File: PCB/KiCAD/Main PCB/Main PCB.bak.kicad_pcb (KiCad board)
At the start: 2 copper layers, 120 x 120 mm, 144 parts, among them IC1 ADG608BRZ, IC2 ADG608BRZ, IC3 XB3-24Z8CM, J1 Conn_01x02, J2 Conn_01x02, J3 Conn_01x02, J4 Conn_Coaxial_Small, J5 Conn_01x02, J6 Conn_01x04, J7 Conn_01x04, M1 Conn_01x02_Pin, M2 Conn_01x02_Pin, M3 Conn_01x02_Pin, M4 Conn_01x02_Pin, Q1 BSS138, Q2 BSS138, U2 Teensy4.1, U3 Teensy4.0, U4 LMD18200, U5 LMD18200, U6 LMD18200, U7 LMD18200, U8 MIC5219-3.3YM5

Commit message: Changes to the main PCB
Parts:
- moved J6 4.50 mm to (-29.5, 31.0)
- moved J7 4.50 mm to (23.5, 31.0)
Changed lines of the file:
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@@
 	(footprint "Connector_JST:JST_PH_B4B-PH-K_1x04_P2.00mm_Vertical"
 		(layer "B.Cu")
-		(at -29.5 26.5)
+		(at -29.5 31)
 		(descr "JST PH series connector, B4B-PH-K (http://www.jst-mfg.com/product/pdf/eng/ePH.pdf), generated with kicad-footprint-generator")
 		(tags "connector JST PH side entry")
@@
 	(footprint "Connector_JST:JST_PH_B4B-PH-K_1x04_P2.00mm_Vertical"
 		(layer "B.Cu")
-		(at 23.5 26.5)
+		(at 23.5 31)
 		(descr "JST PH series connector, B4B-PH-K (http://www.jst-mfg.com/product/pdf/eng/ePH.pdf), generated with kicad-footprint-generator")
 		(tags "connector JST PH side entry")

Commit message: Updated to main PCB
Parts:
- added J8: Conn_01x04, Connector_JST:JST_PH_B4B-PH-K_1x04_P2.00mm_Vertical, F.Cu at (29.0, 14.5)
- moved J6 4.50 mm to (-29.5, 26.5)
- moved J7 4.50 mm to (23.5, 26.5)
- turned D10 to 158 degrees
- turned D12 to 113 degrees
- turned D14 to 68 degrees
- turned D16 to 23 degrees
- turned D18 to -22 degrees
- turned D20 to -67 degrees
- turned D22 to -112 degrees
- turned D24 to -157 degrees
- turned IR10 to -22 degrees
- turned IR12 to -67 degrees
- turned IR14 to -112 degrees
- turned IR16 to -157 degrees
- turned IR2 to 158 degrees
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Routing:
- net GND: track 77.1 -> 964.7 mm, vias 0 -> 1
- net TSSP_PWR: track 0.00 -> 410.8 mm, vias 0 -> 4
- net +3V3: track 0.00 -> 215.3 mm, vias 0 -> 6
- net +5V: track 0.00 -> 163.3 mm, vias 0 -> 3
- net IR_DIR_157.5: track 0.00 -> 158.9 mm, vias 0 -> 3
- net LG_RECEIVE: track 0.00 -> 154.4 mm, vias 0 -> 6
- net +3V3_4_0: track 0.00 -> 147.5 mm, vias 0 -> 8
- net START_BUTTON: track 0.00 -> 137.2 mm, vias 0 -> 2
- net LED_2_A2: track 0.00 -> 134.7 mm, vias 0 -> 2
- net +3V3_4_1: track 0.00 -> 132.3 mm, vias 0 -> 5
- net 3V3_SDA: track 0.00 -> 125.4 mm, vias 0 -> 3
- net IR_DIR_112.5: track 0.00 -> 119.7 mm, vias 0 -> 1
- net IR_DIR_180: track 0.00 -> 119.6 mm, vias 0 -> 4
- net 3V3_SCL: track 0.00 -> 114.3 mm, vias 0 -> 4
- net CAMERA_TX: track 0.00 -> 109.3 mm, vias 0 -> 3
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- removed copper zone on B.Cu, net GND
- removed copper zone on F.Cu, net GND

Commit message: More PCB updates
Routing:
- net Net-(IC2-S3): track 64.7 -> 65.7 mm
- net START_BUTTON: track 137.2 -> 136.2 mm
- net MOTOR_4_SPEED: track 60.3 -> 61.3 mm
- net MOTOR_3_SPEED: track 65.4 -> 64.6 mm
- net LED_1_A0: track 86.2 -> 86.9 mm
- net Net-(IC1-S4): track 59.3 -> 59.9 mm
- net Net-(IC1-S1): track 55.2 -> 55.9 mm
- net LED_2_A1: track 104.7 -> 104.1 mm

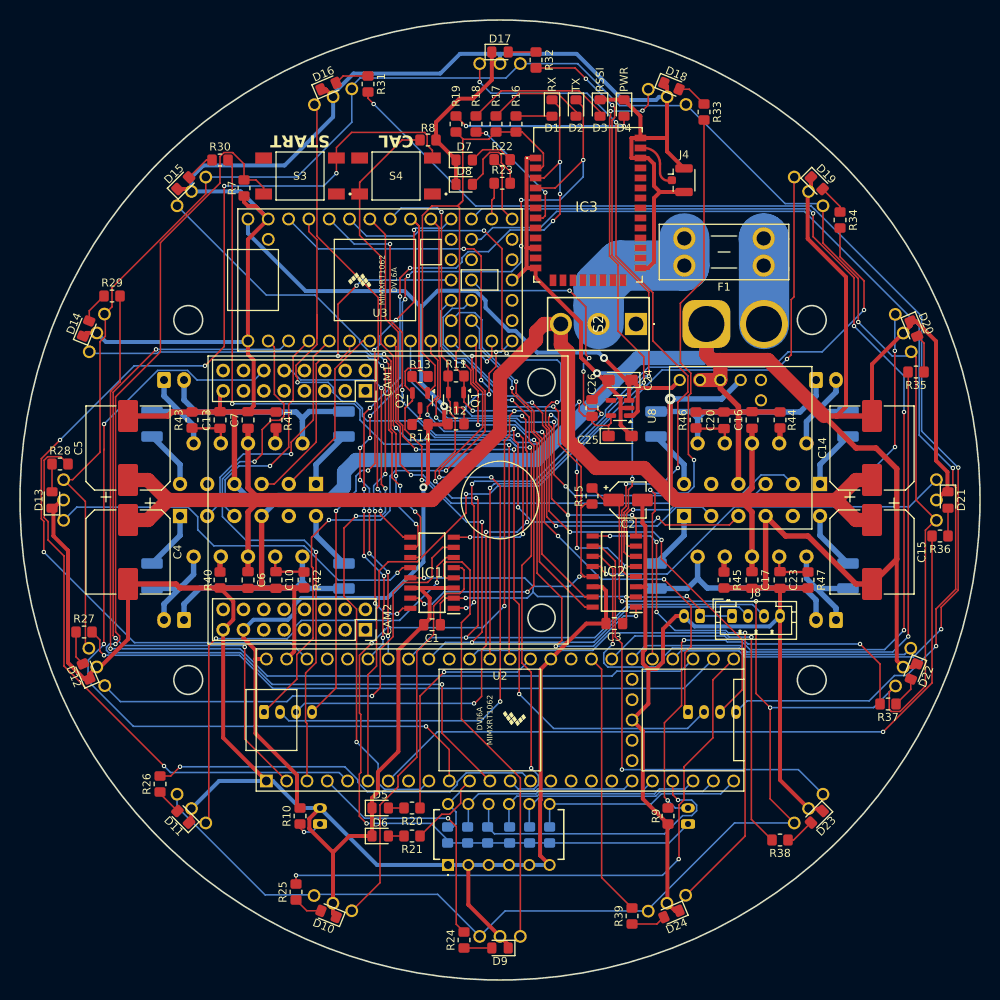
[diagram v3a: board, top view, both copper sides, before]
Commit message: The Main PCB is now curved
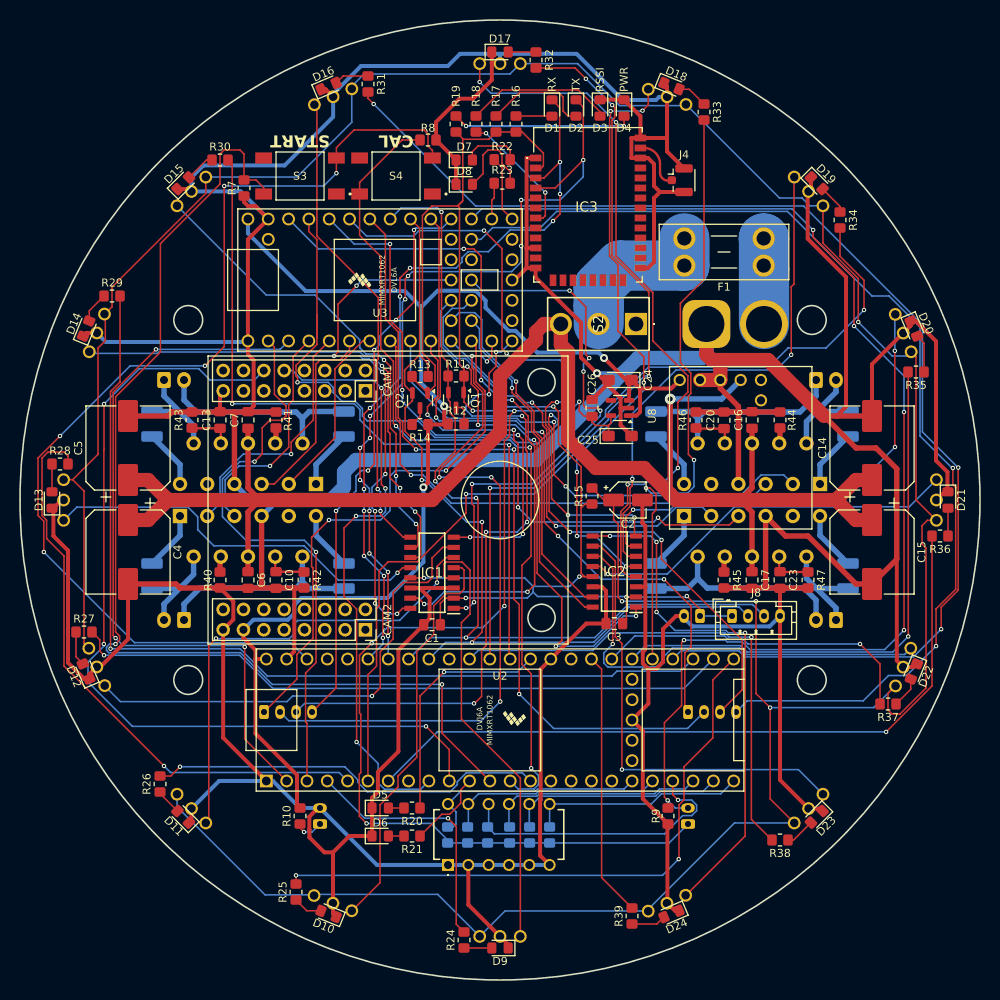
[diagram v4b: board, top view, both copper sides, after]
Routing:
- net 3V3_SDA: track 125.4 -> 107.0 mm
- net CAMERA_TX: track 109.3 -> 111.0 mm
- net Net-(D7-A): track 5.76 -> 7.46 mm
- net TSSP_PWR: track 410.8 -> 412.4 mm
- net IR_DIR_90: track 71.7 -> 73.3 mm
- net IR_DIR_202.5: track 75.5 -> 77.0 mm
- net LG_RECEIVE: track 154.4 -> 153.2 mm
- net START_BUTTON: track 136.2 -> 137.3 mm
- net +3V3_4_1: track 132.3 -> 133.3 mm
- net Net-(IC2-S3): track 65.7 -> 64.8 mm
- net GND: track 964.7 -> 965.6 mm
- net Net-(IC2-S2): track 75.3 -> 74.4 mm
- net Net-(D2-A): track 12.7 -> 13.5 mm
- net LED_2_A1: track 104.1 -> 104.9 mm
- net Net-(D8-A): track 10.5 -> 11.1 mm
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
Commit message: Added a dribbler motor controller
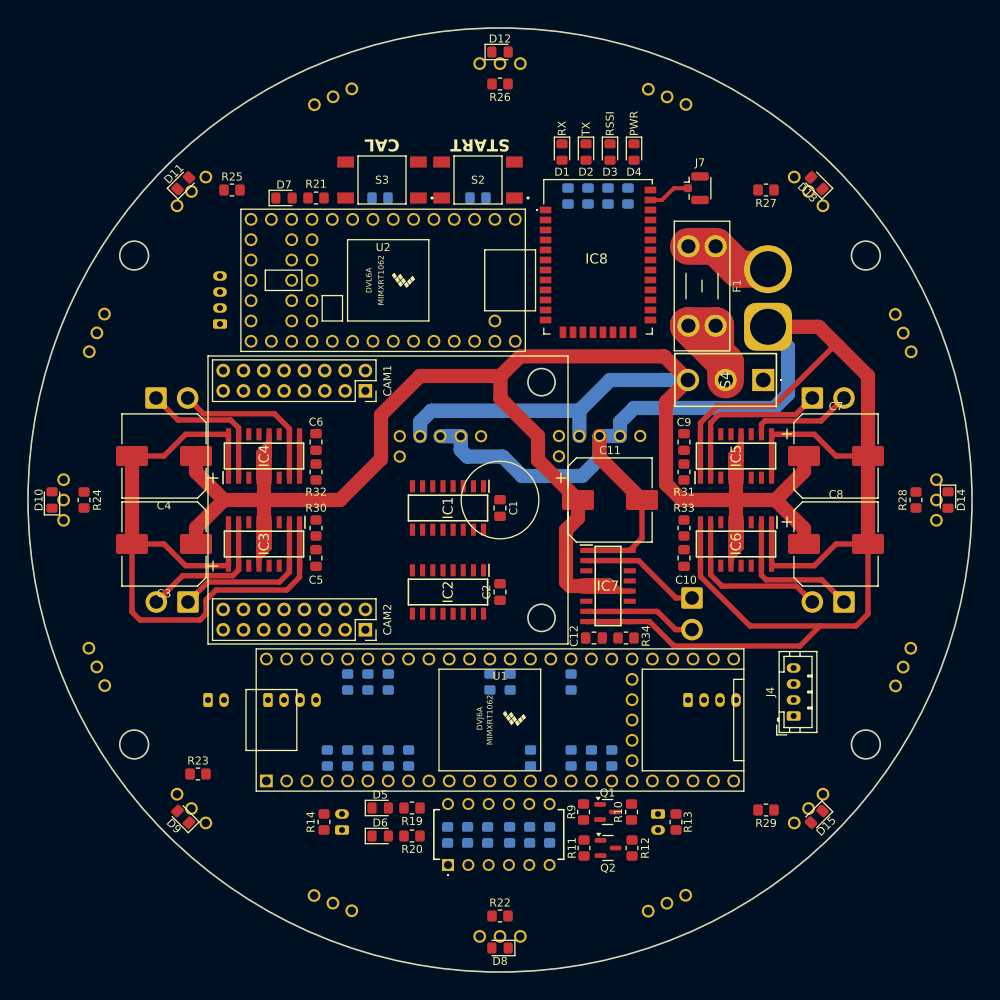
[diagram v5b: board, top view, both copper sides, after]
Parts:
- removed C13, C16, C17, C20, C23, C26: 0.1uF, Capacitor_SMD:C_0805_2012Metric_Pad1.18x1.45mm_HandSolder
- removed C14, C15: 220uF, Capacitor_SMD:CP_Elec_10x10
- removed C18, C19, C21, C22: 10nF, Capacitor_SMD:C_1210_3225Metric_Pad1.33x2.70mm_HandSolder
- removed the C2 at (16.0, 0.00)
- removed C24, C25: 10uF, Capacitor_Tantalum_SMD:CP_EIA-3216-12_Kemet-S_Pad1.58x1.35mm_HandSolder
- removed the D10 at (-21.4, 51.7)
- removed the D12 at (-51.7, 21.4)
- removed the D14 at (-51.7, -21.4)
- removed D16, D18, D20, D22, D24: BALL_DIR_LED, LED_SMD:LED_0805_2012Metric_Pad1.15x1.40mm_HandSolder
- removed the D7 at (-4.47, -42.5)
- removed the J1 at (25.8, -22.0)
- removed the J5 at (25.0, 14.5)
- removed the R15 at (11.5, -0.50)
- removed the R22 at (0.27, -42.5)
- removed the R25 at (-25.5, 49.0)
- removed the R27 at (-52.0, 16.5)
- removed the R29 at (-48.5, -25.5)
- removed the S2 at (17.0, -22.0)
- removed the U1 at (30.0, -5.88)
- removed U5, U6, U7: LMD18200, Package_TO_SOT_THT:TO-220-11_P3.4x5.08mm_StaggerOdd_Lead4.58mm_Vertical
- removed U8: MIC5219-3.3YM5, Package_TO_SOT_SMD:SOT-23-5
- added C4: 220uF, Capacitor_SMD:CP_Elec_10x10, F.Cu at (-42.0, -5.50)
- added DRIBBLER1: Conn_01x02, Connector_JST:JST_VH_B2P-VH-B_1x02_P3.96mm_Vertical, B.Cu at (24.0, 12.2)
- added IC3: VNH7070ASTR, VNH7070ASTR:SOIC127P600X175-16N, F.Cu at (-29.5, 5.50)
- added IC4: VNH7070ASTR, VNH7070ASTR:SOIC127P600X175-16N, F.Cu at (-29.5, -5.50)
- added IC5: VNH7070ASTR, VNH7070ASTR:SOIC127P600X175-16N, F.Cu at (29.5, -5.50)
- added IC6: VNH7070ASTR, VNH7070ASTR:SOIC127P600X175-16N, F.Cu at (29.5, 5.50)
- added IC7: VNH7070ASTR, VNH7070ASTR:SOIC127P600X175-16N, F.Cu at (13.5, 10.8)
- added J3: Conn_01x04, Connector_JST:JST_PH_B4B-PH-K_1x04_P2.00mm_Vertical, B.Cu at (23.5, 25.0)
- added J8: Conn_01x02, Connector_AMASS:AMASS_XT60-M_1x02_P7.20mm_Vertical, B.Cu at (33.5, -21.6)
- added J9: Conn_01x02, Connector_JST:JST_PH_B2B-PH-K_1x02_P2.00mm_Vertical, B.Cu at (-36.5, 25.0)
- added R32: 1k, Resistor_SMD:R_0805_2012Metric_Pad1.20x1.40mm_HandSolder, F.Cu at (-23.0, -3.50)
- added R34: 1k, Resistor_SMD:R_0805_2012Metric_Pad1.20x1.40mm_HandSolder, F.Cu at (15.8, 17.2)
- added R36: 1k, Resistor_SMD:R_0805_2012Metric_Pad1.20x1.40mm_HandSolder, B.Cu at (-19.1, 32.2)
- added R38: 1k, Resistor_SMD:R_0805_2012Metric_Pad1.20x1.40mm_HandSolder, B.Cu at (-14.0, 32.2)
- added R42: 1k, Resistor_SMD:R_0805_2012Metric_Pad1.20x1.40mm_HandSolder, B.Cu at (11.4, 32.2)
- added R48: 1k, Resistor_SMD:R_0805_2012Metric_Pad1.20x1.40mm_HandSolder, B.Cu at (8.89, 22.8)
- added R49: 1k, Resistor_SMD:R_0805_2012Metric_Pad1.20x1.40mm_HandSolder, B.Cu at (1.27, 22.8)
- added S4: 1101M2S3CGE2, 1101M2S3CGE2:1101M2S3CGE2, F.Cu at (32.9, -15.0)
- added U3: ~, Pololu:D36V28F3, B.Cu at (10.0, 1.12)
- C10, C6: value 0.1uF -> 33nF
- C11, C8: value 10nF -> 220uF; footprint Capacitor_SMD:C_1210_3225Metric_Pad1.33x2.70mm_HandSolder -> Capacitor_SMD:CP_Elec_10x10; moved to F.Cu
- C12, C9: value 10nF -> 33nF; footprint Capacitor_SMD:C_1210_3225Metric_Pad1.33x2.70mm_HandSolder -> Capacitor_SMD:C_0805_2012Metric_Pad1.18x1.45mm_HandSolder; moved to F.Cu
- C5: value 220uF -> 33nF; footprint Capacitor_SMD:CP_Elec_10x10 -> Capacitor_SMD:C_0805_2012Metric_Pad1.18x1.45mm_HandSolder
- C7: value 0.1uF -> 220uF; footprint Capacitor_SMD:C_0805_2012Metric_Pad1.18x1.45mm_HandSolder -> Capacitor_SMD:CP_Elec_10x10
- M1, M2, M3, M4: value Conn_01x02_Pin -> Conn_01x02; footprint Connector_JST:JST_XH_B2B-XH-A_1x02_P2.50mm_Vertical -> Connector_JST:JST_VH_B2P-VH-B_1x02_P3.96mm_Vertical
- R15: renamed from R16; moved to B.Cu
- R16: renamed from R17; moved to B.Cu
- R17: renamed from R18; moved to B.Cu
- R18: renamed from R19; moved to B.Cu
- R3: renamed from R7; moved to B.Cu
- R30: renamed from R42; value 2.7k -> 1k
- R31, R33: value 130 -> 1k
- R35, R37, R39: value 130 -> 1k; moved to B.Cu
- R4: renamed from R8; moved to B.Cu
- R40, R41, R44, R45: value 0 -> 1k; moved to B.Cu
- R43, R46, R47: value 2.7k -> 1k; moved to B.Cu
- U4: value LMD18200 -> ~; footprint Package_TO_SOT_THT:TO-220-11_P3.4x5.08mm_StaggerOdd_Lead4.58mm_Vertical -> Pololu:D36V28F5
- moved R35 88.0 mm to (-21.6, 32.2), turned to -90 degrees
- moved C8 85.6 mm to (42.0, 5.50), turned to 0 degrees
- moved J2 76.0 mm to (-35.0, -22.0), turned to 90 degrees
- moved C7 73.6 mm to (42.0, -5.50), turned to 0 degrees
- moved R37 65.4 mm to (-16.5, 32.2), turned to -90 degrees
- moved R44 63.2 mm to (-19.1, 22.8), turned to -90 degrees
- moved R31 62.5 mm to (23.0, -3.50), turned to 90 degrees
- moved R11 62.4 mm to (10.5, 43.5), turned to 90 degrees
- moved C12 61.4 mm to (11.8, 17.2), turned to 180 degrees
- moved Q2 60.7 mm to (13.5, 43.5), turned to 0 degrees
- moved R43 59.8 mm to (3.81, 32.2), turned to -90 degrees
- moved R41 59.6 mm to (14.0, 32.2), turned to -90 degrees
- moved R12 59.2 mm to (16.5, 43.5), turned to -90 degrees
- moved R9 56.8 mm to (10.4, 39.0), turned to -90 degrees
- moved Q1 54.9 mm to (13.4, 39.0), turned to 0 degrees
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- renumbered C3 to C2, C4 to C3, D13 to D10, D15 to D11, D17 to D12, D19 to D13, D21 to D14, D23 to D15, D8 to D7, D9 to D8, D11 to D9, IC3 to IC8, J6 to J1, J7 to J2, J8 to J4, J2 to J5, J3 to J6, J4 to J7, R12 to R10, R13 to R11, R14 to R12, R9 to R13, R10 to R14, R20 to R19, R21 to R20, R23 to R21, R24 to R22, R26 to R23, R28 to R24, R30 to R25, R32 to R26, R34 to R27, R36 to R28, R38 to R29, R3 to R5, R4 to R6, R5 to R7, R6 to R8, R11 to R9, S3 to S2, S4 to S3, U2 to U1, U3 to U2
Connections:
- net STATUS_GREEN_4_1 renamed STATUS_GREEN_MAIN
- net STATUS_RED_4_1 renamed STATUS_RED_MAIN
- net TEENSY_RX renamed TEENSY_1_RX
- net TEENSY_TX renamed TEENSY_1_TX
- C1 pad 1: +3V3_4_0 -> +3V3
- C10 pad 1: Net-(U4-CURRENT_SENSE_OUTPUT) -> Net-(IC6-CS)
- C11 pad 1: Net-(M2-Pin_2) -> +12V
- C11 pad 2: Net-(U5-BOOTSTRAP1) -> GND
- C12 pad 2: Net-(M2-Pin_1) -> GND
- C2 pad 1: +3V3_4_0 -> +3V3
- C5 pad 1: +12V -> Net-(IC3-CS)
- C6 pad 1: +12V -> Net-(IC4-CS)
- C8 pad 1: Net-(M1-Pin_2) -> +12V
- C8 pad 2: Net-(U4-BOOTSTRAP1) -> GND
- C9 pad 1: Net-(U4-BOOTSTRAP2) -> Net-(IC5-CS)
- C9 pad 2: Net-(M1-Pin_1) -> GND
- IC1 pad 13: +3V3_4_0 -> +3V3
- IC1 pad 2: +3V3_4_0 -> +3V3
- IC2 pad 13: +3V3_4_0 -> +3V3
- IC2 pad 2: +3V3_4_0 -> +3V3
- J4 pad 1: +3V3_4_0 -> +3V3
- M1 pad 1: Net-(M1-Pin_1) -> OUT_A_M1
- M1 pad 2: Net-(M1-Pin_2) -> OUT_B_M1
- M2 pad 1: Net-(M2-Pin_1) -> OUT_A_M2
- M2 pad 2: Net-(M2-Pin_2) -> OUT_B_M2
- M3 pad 1: Net-(M3-Pin_1) -> OUT_A_M3
- M3 pad 2: Net-(M3-Pin_2) -> OUT_B_M3
- M4 pad 1: Net-(M4-Pin_1) -> OUT_A_M4
- M4 pad 2: Net-(M4-Pin_2) -> OUT_B_M4
- R1 pad 1: +3V3 -> Net-(U1-27_A13_SCK1)
- R1 pad 2: Net-(U2-27_A13_SCK1) -> +3V3
- R2 pad 1: +3V3 -> Net-(U1-28_RX7)
- R2 pad 2: Net-(U2-28_RX7) -> +3V3
- R21 pad 1: STATUS_GREEN_4_0 -> STATUS_GREEN_TEENSY_1
- R30 pad 1: Net-(U4-CURRENT_SENSE_OUTPUT) -> Net-(IC3-CS)
- R31 pad 1: Net-(D16-A) -> Net-(IC4-CS)
- R31 pad 2: IR_DIR_157.5 -> GND
- R33 pad 1: Net-(D18-A) -> Net-(IC6-CS)
- R33 pad 2: IR_DIR_202.5 -> GND
- R35 pad 1: Net-(D20-A) -> PWM_M1
- R35 pad 2: IR_DIR_247.5 -> Net-(U1-2_OUT2)
- R37 pad 1: Net-(D22-A) -> IN_B_M1
- R37 pad 2: IR_DIR_292.5 -> Net-(U1-4_BCLK2)
- R39 pad 1: Net-(D24-A) -> IN_B_M2
- R39 pad 2: IR_DIR_337.5 -> Net-(U1-6_OUT1D)
- R40 pad 1: MOTOR_1_BRAKE -> PWM_M4
- R40 pad 2: GND -> Net-(U1-24_A10_TX6_SCL2)
- R41 pad 1: MOTOR_2_BRAKE -> IN_B_M4
- R41 pad 2: GND -> Net-(U1-26_A12_MOSI1)
- R43 pad 1: Net-(U5-CURRENT_SENSE_OUTPUT) -> PWM_M2
- R43 pad 2: GND -> Net-(U1-12_MISO_MQSL)
- R44 pad 1: MOTOR_3_BRAKE -> Net-(U1-23_A9_CRX1_MCLK1)
- R44 pad 2: GND -> PWM_M3
- R45 pad 1: MOTOR_4_BRAKE -> Net-(U1-21_A7_RX5_BCLK1)
- R45 pad 2: GND -> IN_B_M3
- R46 pad 1: Net-(U6-CURRENT_SENSE_OUTPUT) -> Net-(U1-22_A8_CTX1)
- R46 pad 2: GND -> IN_A_M3
- R47 pad 1: Net-(U7-CURRENT_SENSE_OUTPUT) -> Net-(U1-15_A1_RX3_SPDIF_IN)
- R47 pad 2: GND -> PWM_DRIB
- R5 pad 1: +3V3 -> Net-(U1-29_TX7)
- R5 pad 2: Net-(U2-29_TX7) -> +3V3
- R6 pad 1: +3V3 -> Net-(U1-30_CRX3)
- R6 pad 2: Net-(U2-30_CRX3) -> +3V3
- R7 pad 1: +3V3 -> Net-(U1-31_CTX3)
- R7 pad 2: Net-(U2-31_CTX3) -> +3V3
- R8 pad 1: +3V3 -> Net-(U1-32_OUT1B)
- R8 pad 2: Net-(U2-32_OUT1B) -> +3V3
- S1 pad B1: Net-(U2-27_A13_SCK1) -> Net-(U1-27_A13_SCK1)
- S1 pad B2: Net-(U2-28_RX7) -> Net-(U1-28_RX7)
- S1 pad B3: Net-(U2-29_TX7) -> Net-(U1-29_TX7)
- S1 pad B4: Net-(U2-30_CRX3) -> Net-(U1-30_CRX3)
- S1 pad B5: Net-(U2-31_CTX3) -> Net-(U1-31_CTX3)
- S1 pad B6: Net-(U2-32_OUT1B) -> Net-(U1-32_OUT1B)
- S2 pad 2: +3V3_4_1 -> +3V3
- S3 pad 2: +3V3_4_1 -> +3V3
- U1 pad 14: IR_DIR_45 -> Net-(U1-12_MISO_MQSL)
- U1 pad 16: unconnected-(U2-24_A10_TX6_SCL2-Pad16) -> Net-(U1-24_A10_TX6_SCL2)
- U1 pad 17: unconnected-(U2-25_A11_RX6_SDA2-Pad17) -> Net-(U1-25_A11_RX6_SDA2)
- U1 pad 18: unconnected-(U2-26_A12_MOSI1-Pad18) -> Net-(U1-26_A12_MOSI1)
- U1 pad 19: Net-(U2-27_A13_SCK1) -> Net-(U1-27_A13_SCK1)
- U1 pad 20: Net-(U2-28_RX7) -> Net-(U1-28_RX7)
- U1 pad 21: Net-(U2-29_TX7) -> Net-(U1-29_TX7)
- U1 pad 22: Net-(U2-30_CRX3) -> Net-(U1-30_CRX3)
- U1 pad 23: Net-(U2-31_CTX3) -> Net-(U1-31_CTX3)
- U1 pad 24: Net-(U2-32_OUT1B) -> Net-(U1-32_OUT1B)
- U1 pad 25: IR_DIR_22.5 -> IR_DIR_0
- U1 pad 26: IR_DIR_67.5 -> IR_DIR_90
- U1 pad 27: IR_DIR_112.5 -> IR_DIR_180
- U1 pad 28: IR_DIR_157.5 -> IR_DIR_270
- U1 pad 29: IR_DIR_202.5 -> IR_DIR_45
- U1 pad 30: IR_DIR_247.5 -> IR_DIR_135
- U1 pad 31: IR_DIR_292.5 -> IR_DIR_225
- U1 pad 32: IR_DIR_337.5 -> IR_DIR_315
- U1 pad 33: unconnected-(U2-41_A17-Pad33) -> Net-(U1-41_A17)
- U1 pad 36: IR_DIR_135 -> Net-(U1-14_A0_TX3_SPDIF_OUT)
- U1 pad 37: IR_DIR_225 -> Net-(U1-15_A1_RX3_SPDIF_IN)
- U1 pad 38: IR_DIR_315 -> COM_RX
- U1 pad 39: unconnected-(U2-17_A3_TX4_SDA1-Pad39) -> COM_TX
- U1 pad 4: IR_DIR_0 -> Net-(U1-2_OUT2)
- U1 pad 42: COM_TX -> LG_RECEIVE
- U1 pad 43: COM_RX -> Net-(U1-21_A7_RX5_BCLK1)
- U1 pad 44: unconnected-(U2-22_A8_CTX1-Pad44) -> Net-(U1-22_A8_CTX1)
- U1 pad 45: unconnected-(U2-23_A9_CRX1_MCLK1-Pad45) -> Net-(U1-23_A9_CRX1_MCLK1)
- U1 pad 46: +3V3_4_1 -> unconnected-(U1-3V3-Pad46)
- U1 pad 5: IR_DIR_90 -> Net-(U1-3_LRCLK2)
- U1 pad 6: IR_DIR_180 -> Net-(U1-4_BCLK2)
- U1 pad 7: IR_DIR_270 -> Net-(U1-5_IN2)
- U1 pad 8: unconnected-(U2-6_OUT1D-Pad8) -> Net-(U1-6_OUT1D)
- U2 pad 10: MOTOR_4_SPEED -> LED_3_A0
- U2 pad 11: MOTOR_4_DIR -> LED_3_A1
- U2 pad 12: LED_1_OUT -> LED_3_A2
- U2 pad 13: LED_1_A0 -> TSSP_1_A0
- U2 pad 14: LED_1_A1 -> TSSP_1_A1
- U2 pad 20: STATUS_RED_4_0 -> STATUS_RED_TEENSY_1
- U2 pad 21: STATUS_GREEN_4_0 -> LED_1_OUT
- U2 pad 22: LG_RECEIVE -> LED_2_OUT
- U2 pad 23: LED_1_A2 -> LED_3_OUT
- U2 pad 24: LED_2_OUT -> TSSP_1_OUT
- U2 pad 27: LED_2_A0 -> TSSP_2_OUT
- U2 pad 28: LED_2_A1 -> TSSP_1_A2
- U2 pad 29: TSSP_1_OUT -> TSSP_2_A0
- U2 pad 30: TSSP_2_OUT -> TSSP_2_A1
- U2 pad 31: +3V3_4_0 -> unconnected-(U2-3V3-Pad31)
- U2 pad 35: LED_2_A2 -> unconnected-(U2-24_A10_TX6_SCL2-Pad35)
- U2 pad 37: unconnected-(U3-26_A12_MOSI1-Pad37) -> TSSP_2_A2
- U2 pad 39: TSSP_1_A0 -> unconnected-(U2-28_RX7-Pad39)
- U2 pad 4: MOTOR_1_SPEED -> LED_1_A0
- U2 pad 40: TSSP_1_A1 -> unconnected-(U2-29_TX7-Pad40)
- U2 pad 41: TSSP_1_A2 -> unconnected-(U2-30_CRX3-Pad41)
- U2 pad 42: TSSP_2_A0 -> unconnected-(U2-31_CTX3-Pad42)
- U2 pad 43: TSSP_2_A1 -> unconnected-(U2-32_OUT1B-Pad43)
- U2 pad 44: TSSP_2_A2 -> unconnected-(U2-33_MCLK2-Pad44)
- U2 pad 5: MOTOR_1_DIR -> LED_1_A1
- U2 pad 6: MOTOR_2_SPEED -> LED_1_A2
- U2 pad 7: MOTOR_2_DIR -> LED_2_A0
- U2 pad 8: MOTOR_3_SPEED -> LED_2_A1
- U2 pad 9: MOTOR_3_DIR -> LED_2_A2
- U4 pad 1: Net-(U4-BOOTSTRAP1) -> unconnected-(U4-PG-Pad1)
- U4 pad 2: Net-(M1-Pin_2) -> unconnected-(U4-EN-Pad2)
- U4 pad 3: MOTOR_1_DIR -> +12V
- U4 pad 4: MOTOR_1_BRAKE -> GND
- U4 pad 5: MOTOR_1_SPEED -> GND
- U4 pad 6: +12V -> +5V
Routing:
- net GND: track 965.6 -> 351.7 mm, vias 1 -> 0
- net TSSP_PWR: track 412.4 -> 0.00 mm, vias 4 -> 0
- net +3V3: track 215.0 -> 0.00 mm, vias 6 -> 0
- net +5V: track 163.5 -> 0.00 mm, vias 3 -> 0
- net IR_DIR_157.5: track 158.3 -> 0.00 mm, vias 3 -> 0
- net LG_RECEIVE: track 153.2 -> 0.00 mm, vias 6 -> 0
- net +3V3_4_0: track 147.1 -> 0.00 mm, vias 8 -> 0
- net START_BUTTON: track 137.3 -> 0.00 mm, vias 2 -> 0
- net LED_2_A2: track 134.7 -> 0.00 mm, vias 2 -> 0
- net +3V3_4_1: track 133.3 -> 0.00 mm, vias 5 -> 0
- net +12V: track 198.6 -> 327.9 mm, vias 1 -> 0
- net IR_DIR_180: track 120.1 -> 0.00 mm, vias 4 -> 0
- net IR_DIR_112.5: track 119.7 -> 0.00 mm, vias 1 -> 0
- net 3V3_SCL: track 114.6 -> 0.00 mm, vias 4 -> 0
- net CAMERA_TX: track 111.0 -> 0.00 mm, vias 3 -> 0
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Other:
- board size 120 x 120 mm -> 118 x 118 mm

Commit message: Added kicker and spare serial and i2c
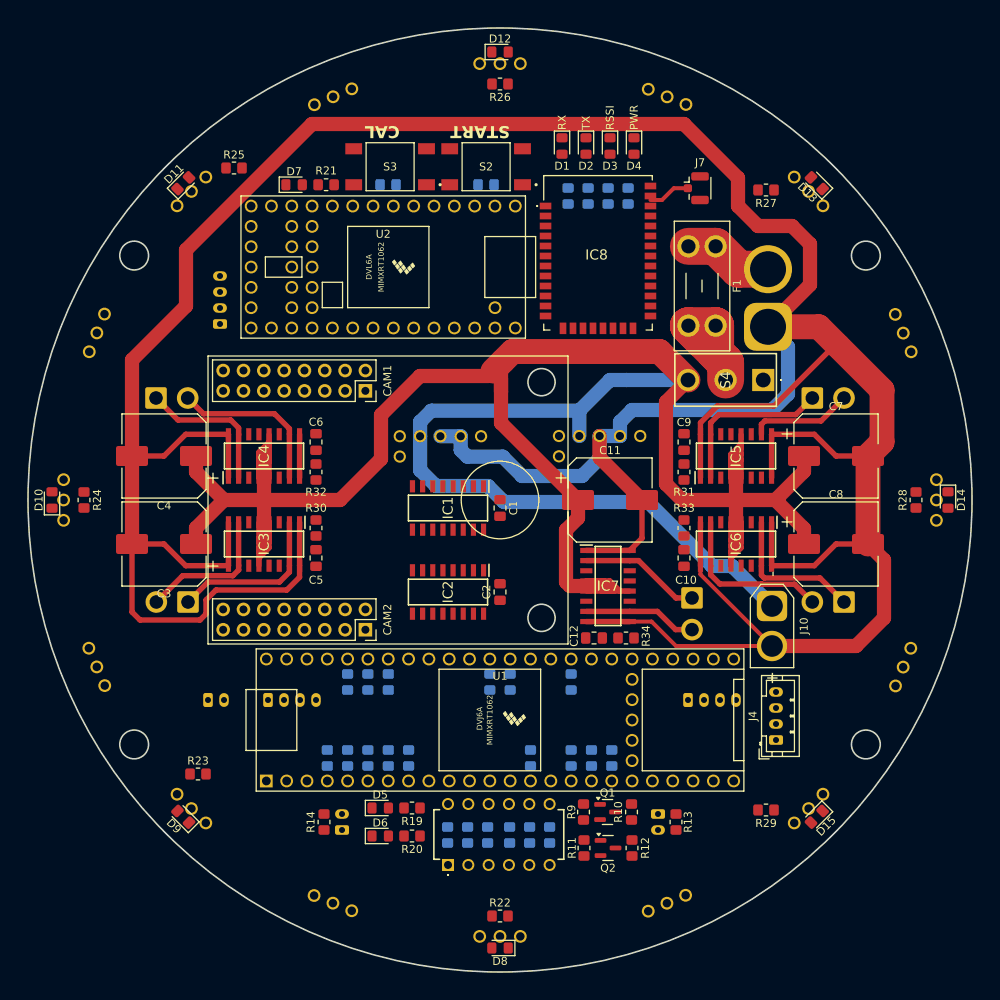
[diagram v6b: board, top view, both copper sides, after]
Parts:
- added J10: Conn_01x02, Connector_AMASS:AMASS_XT30U-M_1x02_P5.0mm_Vertical, F.Cu at (34.0, 13.2)
- moved J4 3.72 mm to (34.5, 30.0)
- moved R25 2.76 mm to (-33.2, -41.5)
- moved D7 2.08 mm to (-25.7, -39.4)
- moved R21 2.08 mm to (-21.7, -39.4)
- moved R3 1.94 mm to (-1.74, -39.4)
- moved S2 1.94 mm to (-1.74, -41.7)
- moved R4 1.94 mm to (-14.0, -39.4)
- moved S3 1.94 mm to (-13.7, -41.7)
- moved U2 1.66 mm to (-14.6, -29.1)
- moved D1 0.75 mm to (7.75, -44.2)
- moved D2 0.75 mm to (10.8, -44.2)
- moved D3 0.75 mm to (13.8, -44.2)
- moved D4 0.75 mm to (16.8, -44.2)
- moved IC8 0.50 mm to (12.2, -23.0)
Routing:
- net GND: track 351.7 -> 485.0 mm
- net +12V: track 327.9 -> 388.7 mm

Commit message: Added a BNO055 and traced PCB (incomplete, no DRC pass)
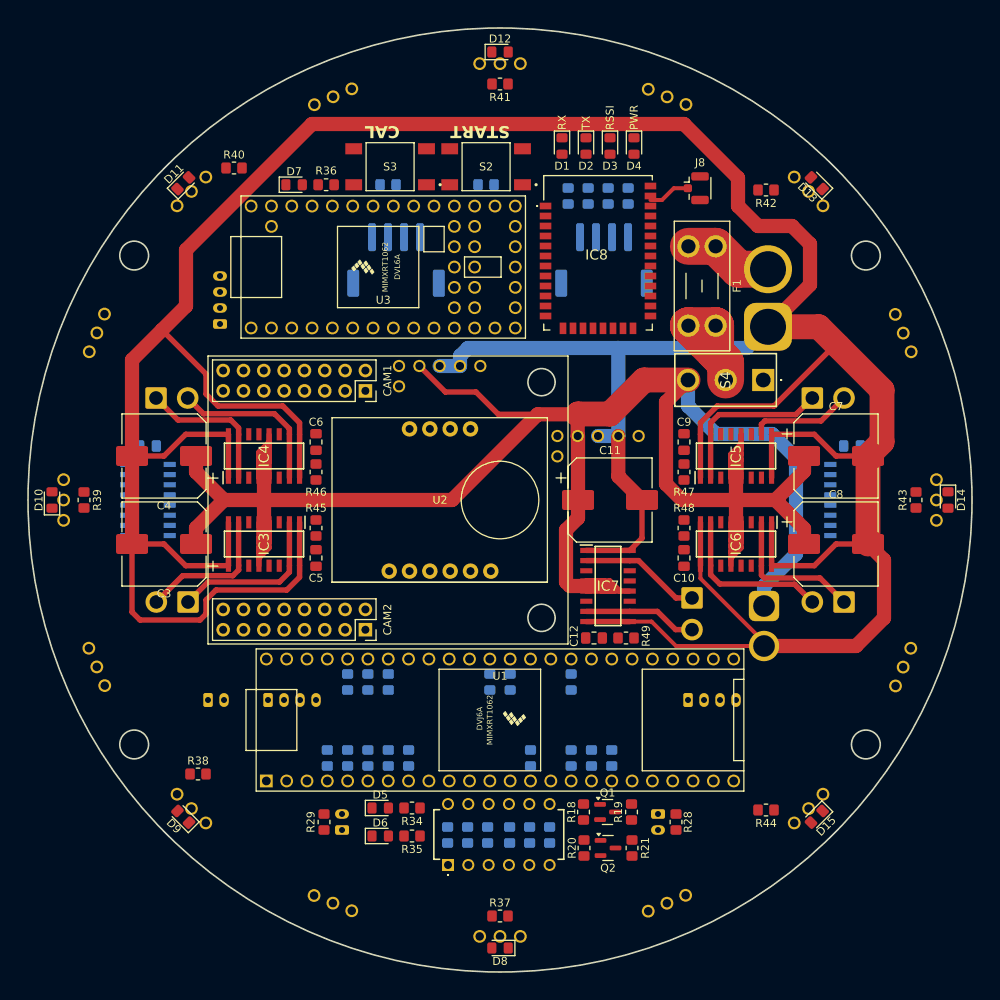
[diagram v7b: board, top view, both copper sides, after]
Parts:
- removed the J4 at (34.5, 30.0)
- added J6: Conn_01x04_MountingPin, Connector_JST:JST_PH_S4B-PH-SM4-TB_1x04-1MP_P2.00mm_Horizontal, B.Cu at (-13.0, -30.0)
- added J7: Conn_01x04_MountingPin, Connector_JST:JST_PH_S4B-PH-SM4-TB_1x04-1MP_P2.00mm_Horizontal, B.Cu at (13.0, -30.0)
- added U2: ~, Adafruit:BNO055, F.Cu at (-7.50, 0.00)
- C1, C2, IC1, IC2: moved to B.Cu
- J11: renamed from J10; moved to B.Cu
- moved IC2 51.8 mm to (44.0, 0.00), turned to 180 degrees
- moved C2 47.6 mm to (44.0, -6.75), turned to 180 degrees
- moved R46 46.0 mm to (-23.0, -3.50), turned to -90 degrees
- moved R47 46.0 mm to (23.0, -3.50), turned to -90 degrees
- moved C1 44.7 mm to (-44.0, -6.75), turned to 180 degrees
- moved IC1 37.5 mm to (-44.0, 0.00), turned to 180 degrees
- moved U5 8.78 mm to (-9.99, -7.62)
- moved J11 1.00 mm to (33.0, 13.2)
- moved U4 0.20 mm to (9.80, 1.12)
- turned C10 to -90 degrees
- turned C5 to -90 degrees
- turned C6 to 90 degrees
- turned C9 to 90 degrees
- turned R45 to 90 degrees
- turned R48 to 90 degrees
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- renumbered J9 to J10, J5 to J4, J6 to J5, J7 to J8, J8 to J9, R6 to R10, R7 to R11, R36 to R12, R38 to R13, R40 to R14, R41 to R15, R8 to R16, R42 to R17, R9 to R18, R10 to R19, R11 to R20, R12 to R21, R44 to R22, R45 to R23, R47 to R24, R46 to R25, R49 to R26, R48 to R27, R13 to R28, R14 to R29, R15 to R30, R16 to R31, R17 to R32, R18 to R33, R19 to R34, R20 to R35, R21 to R36, R22 to R37, R23 to R38, R24 to R39, R25 to R40, R26 to R41, R27 to R42, R28 to R43, R29 to R44, R30 to R45, R31 to R46, R32 to R47, R33 to R48, R34 to R49, R43 to R6, R35 to R7, R37 to R8, R39 to R9, U2 to U3, U3 to U4, U4 to U5
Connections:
- U3 pad 35: unconnected-(U2-24_A10_TX6_SCL2-Pad35) -> SPARE_SCL
- U3 pad 36: unconnected-(U2-25_A11_RX6_SDA2-Pad36) -> SPARE_SDA
- U3 pad 39: unconnected-(U2-28_RX7-Pad39) -> SPARE_RX
- U3 pad 40: unconnected-(U2-29_TX7-Pad40) -> SPARE_TX
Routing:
- net +12V: track 388.7 -> 329.8 mm
- net GND: track 485.0 -> 503.0 mm
